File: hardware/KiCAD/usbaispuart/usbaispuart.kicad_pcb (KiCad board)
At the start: 2 copper layers, 81.5 x 41.7 mm, 52 parts, among them J1 AVR-ISP-UART-PROGRAMER-10, J2 LED Connector, J3 LED Connector, J4 USB_B, J5 Reset Jumper, J6 5V / 3.3 Selection Jumper, J7 Power Out Jumper, Q1 2N2222A, Q2 2N2222A, U1 SN74AHC367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

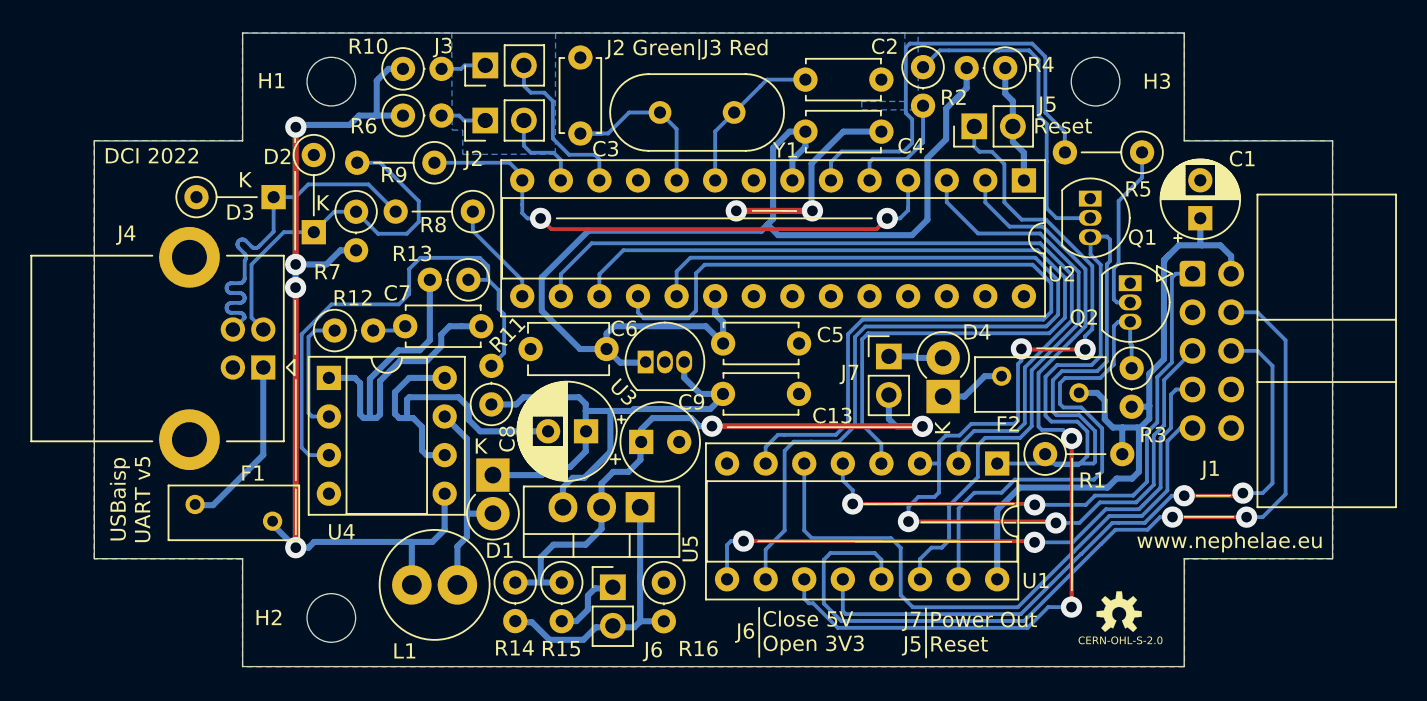
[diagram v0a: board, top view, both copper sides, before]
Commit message: Bump version to 5a. + Fix an error trace. + Change C6 capacitor to electrolytic. + Rearrange layout to reduce noise.
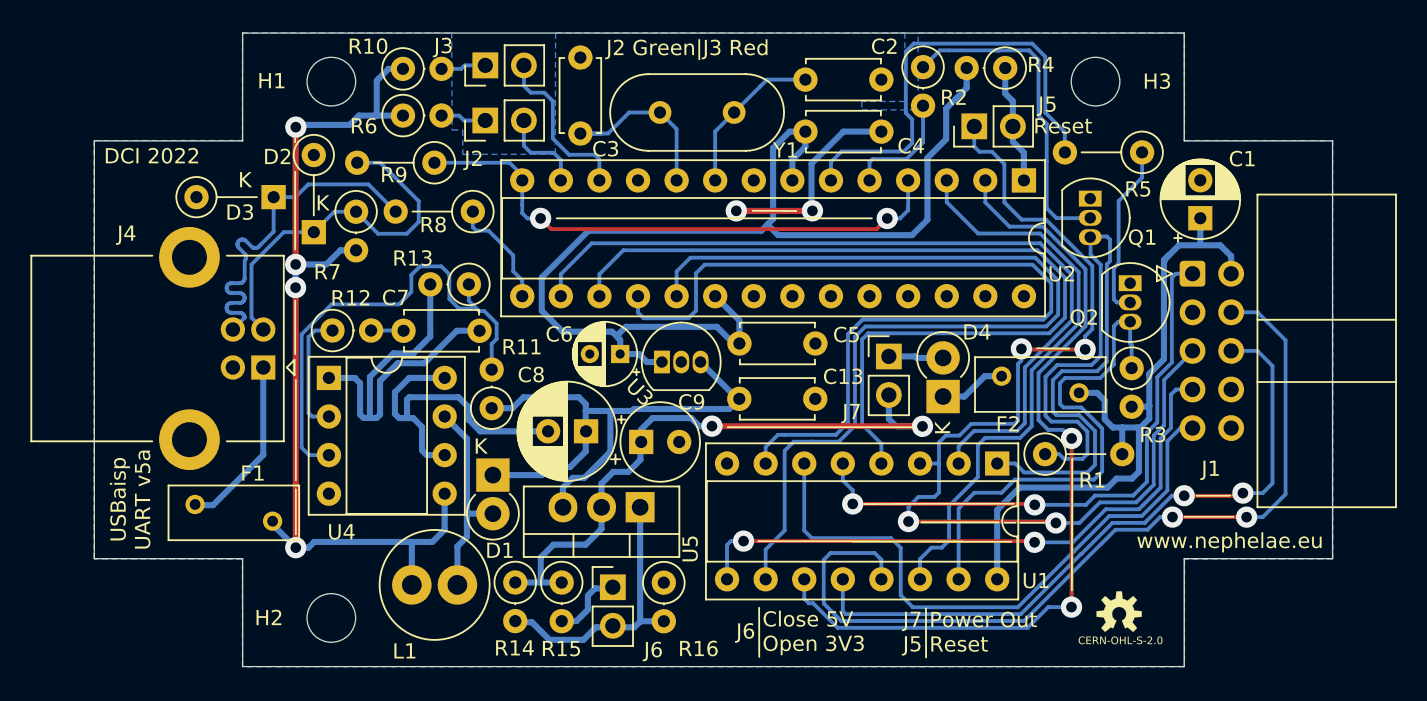
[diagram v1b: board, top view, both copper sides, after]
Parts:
- C6: value 2.2 μF / 16V -> 1 μF / 16V; footprint Capacitor_THT:C_Disc_D5.1mm_W3.2mm_P5.00mm -> Capacitor_THT:CP_Radial_D4.0mm_P2.00mm
- moved C13 1.12 mm to (148.9, 96.9)
- moved C5 1.07 mm to (148.9, 93.3)
- moved U3 1.07 mm to (143.8, 94.5)
- moved C6 0.96 mm to (141.0, 94.0)
- moved C7 0.32 mm to (126.8, 92.5)
- moved R13 0.30 mm to (131.1, 89.4)
- moved R11 0.25 mm to (132.6, 97.5)
- moved R12 0.14 mm to (122.1, 92.4)
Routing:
- net VCC: track 73.1 -> 74.6 mm
- net /REF_1.24V: track 33.7 -> 32.2 mm
- net GND: track 64.1 -> 63.1 mm
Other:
- board text added: "USBaisp UART v5a"
- board text removed: "USBaisp UART v5"

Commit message: Update to 5b
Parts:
- added C10: 0.01 μF, Capacitor_THT:C_Disc_D4.7mm_W2.5mm_P5.00mm, F.Cu at (161.0, 93.3)
- added C11: 10 μF / 25V, Capacitor_THT:CP_Radial_D4.0mm_P1.50mm, F.Cu at (109.6, 104.4)
- added H4: MountingHole, MountingHole:MountingHole_3.2mm_M3_DIN965, F.Cu at (172.3, 111.4)
- C6: value 1 μF / 16V -> 10 μF / 16V; footprint Capacitor_THT:CP_Radial_D4.0mm_P2.00mm -> Capacitor_THT:CP_Radial_D4.0mm_P1.50mm
- D4: footprint Diode_THT:D_DO-41_SOD81_P2.54mm_Vertical_KathodeUp -> Diode_THT:D_DO-41_SOD81_P5.08mm_Vertical_KathodeUp
- moved J7 30.5 mm to (133.9, 111.9), turned to 180 degrees
- moved R16 6.01 mm to (149.1, 112.1), turned to 180 degrees
- moved ? 4.95 mm to (171.9, 106.5)
- moved J6 4.01 mm to (143.6, 111.9), turned to 180 degrees
- moved R15 3.11 mm to (140.3, 109.0)
- moved R14 3.11 mm to (137.2, 109.0)
- moved L1 0.83 mm to (126.8, 108.5)
- moved D4 0.57 mm to (162.8, 96.9), turned to 180 degrees
- moved C6 0.27 mm to (140.8, 94.0)
- moved D1 0.08 mm to (132.7, 101.9)
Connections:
- C9 pad 1: Net-(C9-Pad1) -> /INT_5V_3.3V
- J7 pad 1: /INT_5V_3.3V -> Net-(J7-Pad1)
- J7 pad 2: Net-(C9-Pad1) -> /+6.5V
- R14 pad 1: Net-(C9-Pad1) -> /INT_5V_3.3V
- R15 pad 1: Net-(C9-Pad1) -> /INT_5V_3.3V
- U2 pad 21: (no net) -> Net-(C10-Pad1)
- U5 pad 2: Net-(C9-Pad1) -> /INT_5V_3.3V
- U5 pad 3: /+6.5V -> Net-(J7-Pad1)
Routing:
- net Net-(C9-Pad1): track 40.7 -> 0.00 mm, vias 2 -> 0
- net /INT_5V_3.3V: track 3.61 -> 35.8 mm, vias 0 -> 2
- net Net-(C10-Pad1): track 0.00 -> 17.2 mm
- net Net-(J7-Pad1): track 0.00 -> 9.22 mm
- net VBUS: track 11.6 -> 19.5 mm
- net /+6.5V: track 39.1 -> 46.5 mm
- net MCU_UART_RXD: track 55.1 -> 58.6 mm
- net VCC: track 74.6 -> 76.6 mm
- net MCU_MISO: track 60.7 -> 59.3 mm
- net Net-(J6-Pad1): track 4.81 -> 3.47 mm
- net MCU_MOSI: track 58.8 -> 57.5 mm
- net MCU_SCK: track 64.1 -> 63.1 mm
- net EXT_UART_TXD: track 57.1 -> 58.1 mm
- net Net-(J6-Pad2): track 18.3 -> 17.7 mm
- net /+4.35V: track 61.5 -> 60.8 mm
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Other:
- board text added: "DCI 2023"
- board text added: "J5 J7"
- board text added: "Reset Pwr Out"
- board text added: "USBaisp UART v5b"
- board text removed: "DCI 2022"
- board text removed: "J7 J5"
- board text removed: "Power Out Reset"
- board text removed: "USBaisp UART v5a"
